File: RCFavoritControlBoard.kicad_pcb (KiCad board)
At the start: 2 copper layers, 30 parts, among them J3 Conn_01x03_Pin, U1 SY8303, U2 TPS7A20xxxPDBVR, U3 DRV8833PWP

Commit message: routing done
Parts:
- MOTOR: renamed from 6V MOTOR
- moved R2 1.26 mm to (151.5, 89.3)
- moved D1 1.20 mm to (151.5, 92.7)
- moved C6 1.18 mm to (153.1, 89.3)
- moved C4 1.08 mm to (155.1, 90.0)
- moved VBAT 0.95 mm to (168.8, 86.4)
- moved C5 0.91 mm to (157.6, 90.0)
- moved J3 0.85 mm to (141.6, 78.5)
- moved D3 0.76 mm to (127.7, 84.9)
- moved L1 0.72 mm to (158.0, 82.0)
- moved U1 0.66 mm to (160.7, 91.4)
- moved U3 0.66 mm to (153.9, 100.3)
- moved 5V 0.63 mm to (130.6, 81.1)
- moved R5 0.63 mm to (130.6, 84.1)
- moved H1 0.61 mm to (169.0, 104.0)
- moved C8 0.57 mm to (140.0, 83.5)
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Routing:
- net +6V: track 0.00 -> 82.0 mm, vias 0 -> 4
- net GND: track 0.00 -> 43.3 mm, vias 0 -> 25
- net SERVO_PWM: track 0.00 -> 39.9 mm, vias 0 -> 1
- net DRV8833_IN1: track 0.00 -> 25.4 mm
- net DRV8833_IN2: track 0.00 -> 23.7 mm
- net VBAT: track 0.00 -> 20.7 mm, vias 0 -> 2
- net Motor+: track 0.00 -> 15.3 mm
- net Motor-: track 0.00 -> 15.3 mm
- net Net-(U1-LX): track 0.00 -> 8.68 mm
- net +5V: track 0.00 -> 8.41 mm
- net Net-(U1-FB): track 0.00 -> 5.01 mm
- net Net-(D3-K): track 0.00 -> 3.43 mm
- net Net-(U3-VCP): track 0.00 -> 2.52 mm
- net Net-(U1-FS): track 0.00 -> 2.24 mm
- net Net-(U3-VINT): track 0.00 -> 2.11 mm
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- added copper zone on B.Cu, net GND
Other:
- board outline added: 50.2 x 31.2 mm
- board text added: "Favorit Control Board Rev1"
- board text added: "LiPo 3s"

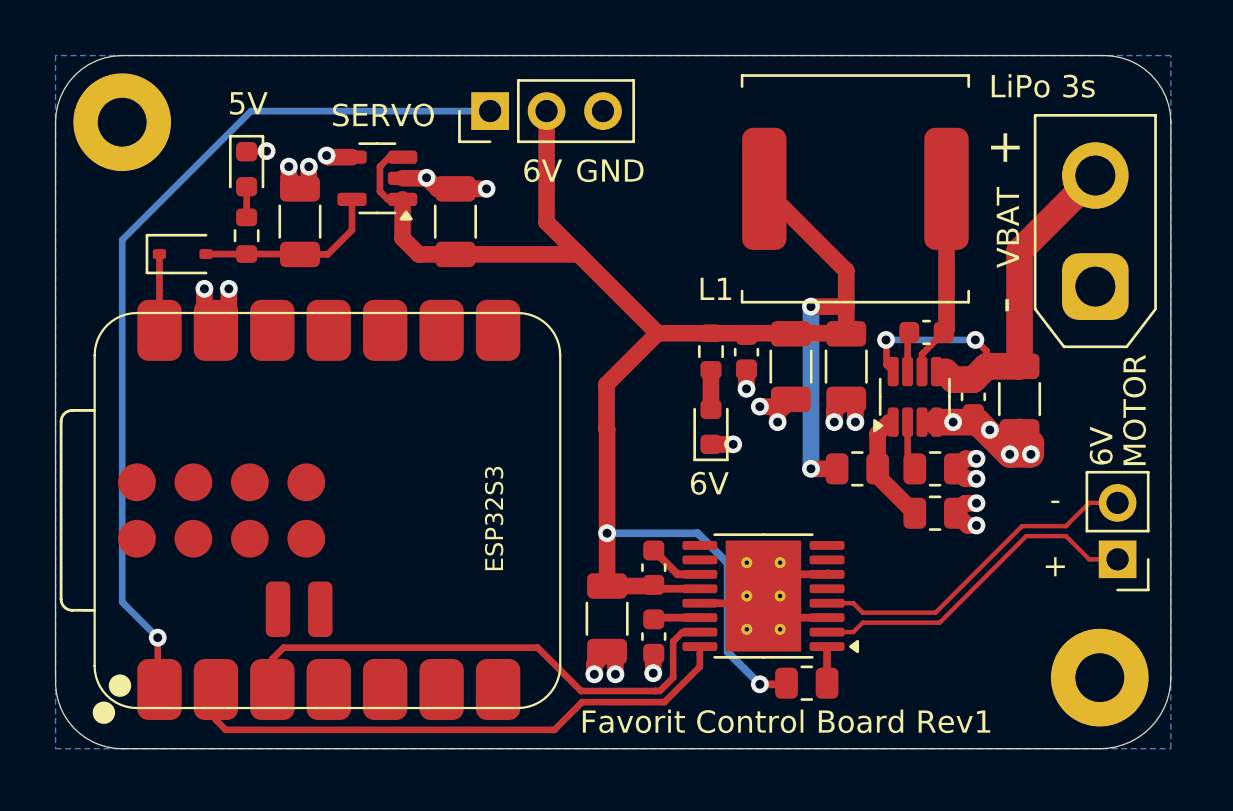
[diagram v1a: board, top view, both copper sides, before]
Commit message: GND is filled in top layer
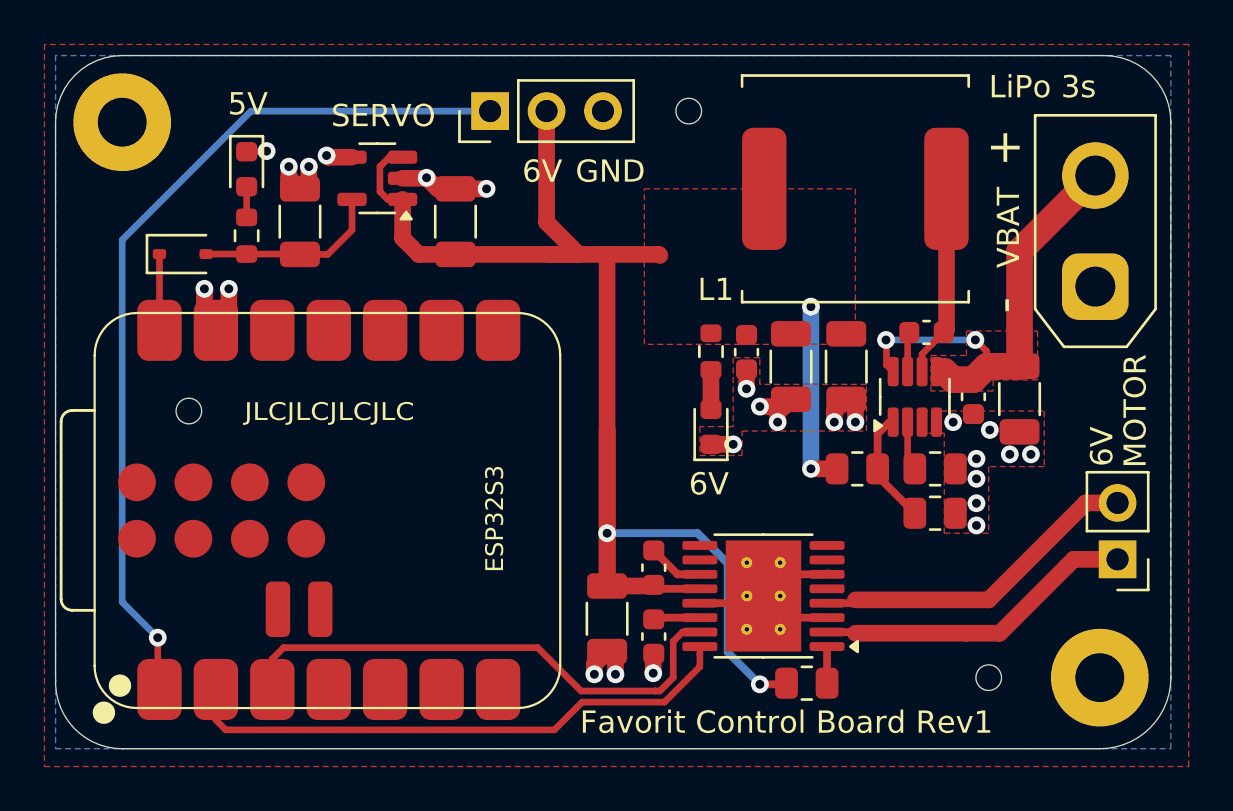
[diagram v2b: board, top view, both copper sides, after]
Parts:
- added REF**: ToolingHole_1.152mm, MountingHole:ToolingHole_1.152mm, F.Cu at (128.0, 92.0)
- added REF**: ToolingHole_1.152mm, MountingHole:ToolingHole_1.152mm, F.Cu at (150.5, 78.5)
- added REF**: ToolingHole_1.152mm, MountingHole:ToolingHole_1.152mm, F.Cu at (164.0, 104.0)
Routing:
- net GND: track 43.3 -> 32.7 mm
- net +6V: track 82.0 -> 73.5 mm
- added copper zone on F.Cu, net +6V
- added copper zone on F.Cu, net GND
- added copper zone on F.Cu, net VBAT
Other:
- board text added: "JLCJLCJLCJLC"
- board text removed: "+"
- board text removed: "-"

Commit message: tried to use Fabrication Toolkit for JLCPCB
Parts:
- renumbered 5V to D2, MOTOR to J1, VBAT to J2, ESP32S3 to U4

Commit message: added logo
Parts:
- removed REF** (x3): ToolingHole_1.152mm, MountingHole:ToolingHole_1.152mm
- added G***: LOGO, logos:logo, F.Cu at (150.5, 78.4)
- renumbered D2 to 5V, U4 to ESP32, J1 to MOTOR, J2 to VBAT
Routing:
- net SERVO_PWM: track 39.9 -> 41.8 mm, vias 1 -> 0
- net GND: vias 25 -> 40
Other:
- board text removed: "JLCJLCJLCJLC"
